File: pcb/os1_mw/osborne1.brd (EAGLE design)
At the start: 147 x 100 mm, 18 parts

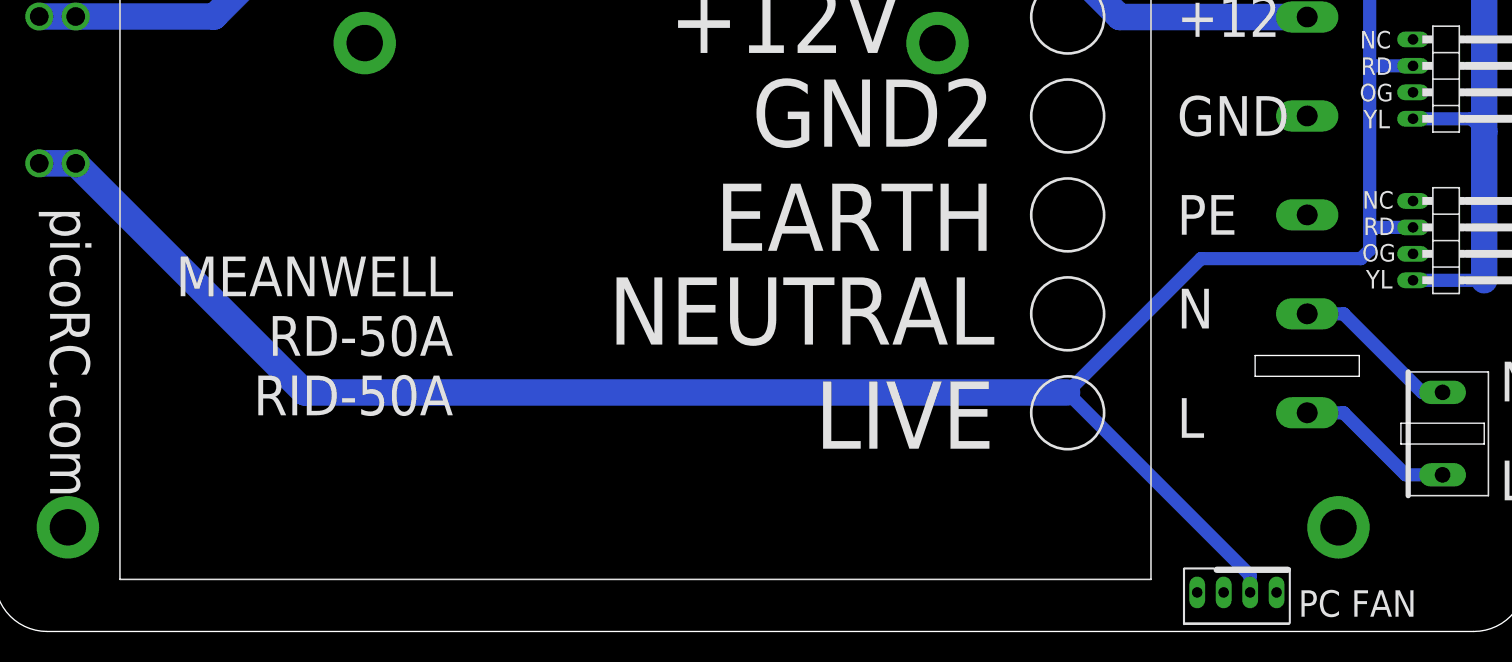
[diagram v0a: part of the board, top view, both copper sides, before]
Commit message: adjust trace spacing
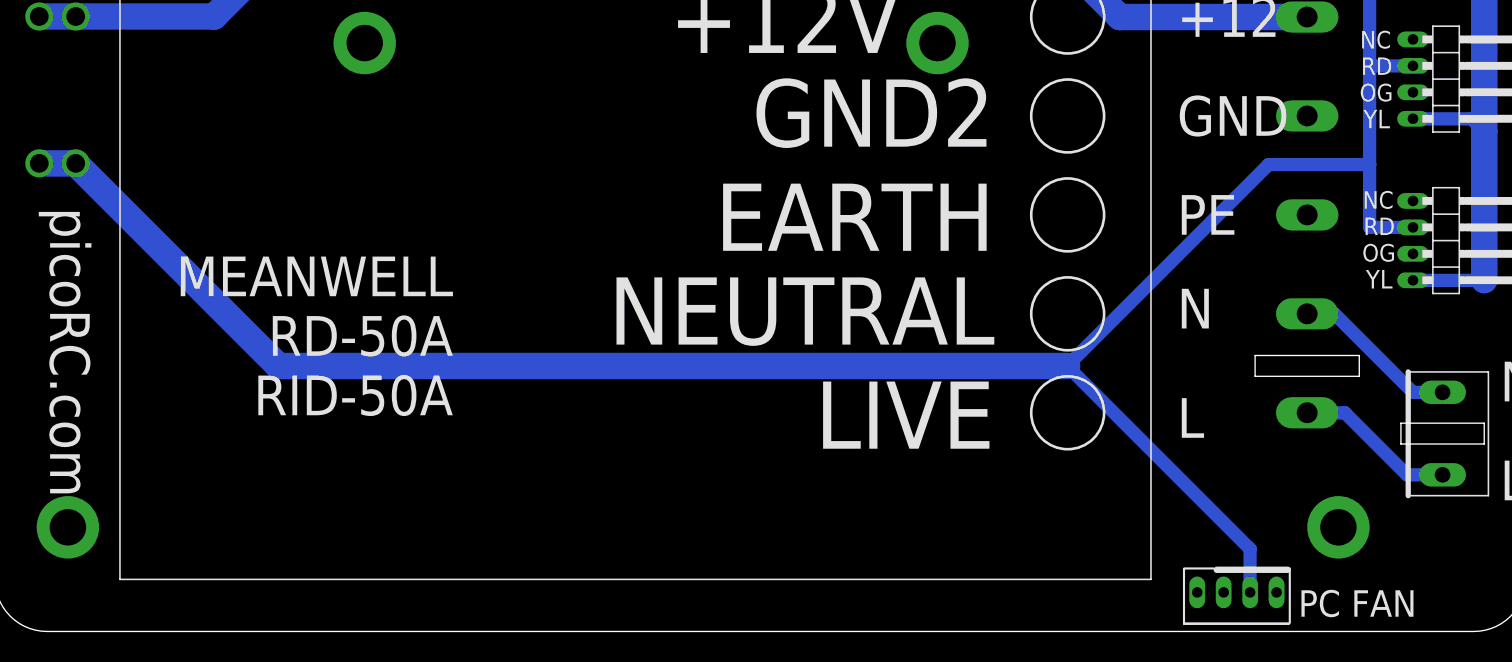
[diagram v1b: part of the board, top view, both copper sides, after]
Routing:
- net +12V: track 213.8 -> 215.4 mm
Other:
- board text added: "YELLOW ORANGE RED NC"
- board text removed: "NC RED ORANGE YELLOW"
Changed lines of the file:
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@@
 <setting verticaltext="up"/>
 </settings>
-<grid distance="5" unitdist="mil" unit="mil" style="lines" multiple="1" display="no" altdistance="1" altunitdist="mil" altunit="mil"/>
+<grid distance="50" unitdist="mil" unit="mil" style="lines" multiple="1" display="no" altdistance="1" altunitdist="mil" altunit="mil"/>
 <layers>
-<layer number="1" name="Top" color="4" fill="1" visible="no" active="yes"/>
+<layer number="1" name="Top" color="4" fill="1" visible="yes" active="yes"/>
 <layer number="2" name="Route2" color="16" fill="1" visible="no" active="no"/>
 <layer number="3" name="Route3" color="17" fill="1" visible="no" active="no"/>
@@
 <text x="132.676" y="54.283" size="1.6764" layer="25" align="center">RD</text>
 <text x="132.565" y="56.823" size="1.6764" layer="25" align="center">NC</text>
-<text x="137.994" y="68.523" size="1.4224" layer="26" distance="80" rot="MR0" align="center-right">NC
+<text x="138.494" y="68.523" size="1.4224" layer="26" distance="80" rot="SMR180" align="center-left">YELLOW
+ORANGE
 RED
-ORANGE
-YELLOW</text>
-<text x="138.121" y="53.013" size="1.4224" layer="26" distance="80" rot="MR0" align="center-right">NC
-RED
-ORANGE
-YELLOW</text>
-<text x="138.248" y="37.503" size="1.4224" layer="26" distance="80" rot="MR0" align="center-right">NC
-RED
-ORANGE
-YELLOW</text>
+NC</text>
 <text x="113.5" y="40" size="3.81" layer="25" align="center-left">PE</text>
 <text x="113.5" y="49.5" size="3.81" layer="25" align="center-left">GND</text>
@@
 <wire x1="123" y1="18" x2="128" y2="18" width="0.508" layer="22"/>
 <wire x1="128" y1="18" x2="135" y2="11" width="0.508" layer="22"/>
-<wire x1="135" y1="11" x2="142" y2="11" width="0.508" layer="22"/>
-<wire x1="142" y1="11" x2="143" y2="12" width="0.508" layer="22"/>
-<wire x1="143" y1="12" x2="143" y2="24" width="0.508" layer="22"/>
-<wire x1="143" y1="24" x2="141" y2="26" width="0.508" layer="22"/>
-<wire x1="141" y1="26" x2="139" y2="26" width="0.508" layer="22"/>
+<wire x1="135" y1="11" x2="142.5" y2="11" width="0.508" layer="22"/>
+<wire x1="142.5" y1="11" x2="143.5" y2="12" width="0.508" layer="22"/>
+<wire x1="143.5" y1="12" x2="143.5" y2="24" width="0.508" layer="22"/>
+<wire x1="143.5" y1="24" x2="141.5" y2="26" width="0.508" layer="22"/>
+<wire x1="141.5" y1="26" x2="139" y2="26" width="0.508" layer="22"/>
 <wire x1="139" y1="26" x2="132" y2="33" width="0.508" layer="22"/>
 <text x="119.5" y="88" size="2.54" layer="25" align="center-left">+</text>
 <text x="134.5" y="85" size="2.54" layer="25" align="center-left">+</text>
 <text x="134.5" y="82" size="2.54" layer="25" align="center-left">+</text>
+<text x="138.494" y="53.023" size="1.4224" layer="26" distance="80" rot="SMR180" align="center-left">YELLOW
+ORANGE
+RED
+NC</text>
+<text x="138.494" y="37.523" size="1.4224" layer="26" distance="80" rot="SMR180" align="center-left">YELLOW
+ORANGE
+RED
+NC</text>
 </plain>
 <attributes>
@@
 <wire x1="136.16" y1="54.31" x2="132.31" y2="54.31" width="1.27" layer="16"/>
 <wire x1="132.31" y1="54.31" x2="132" y2="54" width="1.27" layer="16"/>
-<wire x1="132" y1="36.64" x2="131.16" y2="35.8" width="1.27" layer="16"/>
-<wire x1="132" y1="54" x2="132" y2="38.64" width="1.27" layer="16"/>
-<wire x1="132" y1="38.64" x2="132" y2="36.64" width="1.27" layer="16"/>
-<wire x1="132" y1="38.64" x2="132.16" y2="38.8" width="1.27" layer="16"/>
-<wire x1="132.16" y1="38.8" x2="136.16" y2="38.8" width="1.27" layer="16"/>
 <contactref element="U$7" pad="A1"/>
 <contactref element="U$7" pad="A0"/>
 <wire x1="4.25" y1="44.95" x2="7.75" y2="44.95" width="2.54" layer="16"/>
-<wire x1="102.95" y1="22.95" x2="120.52" y2="5.38" width="1.27" layer="16"/>
-<wire x1="120.52" y1="5.38" x2="120.52" y2="3.75" width="1.27" layer="16"/>
-<wire x1="131.16" y1="35.8" x2="115.8" y2="35.8" width="1.27" layer="16"/>
-<wire x1="115.8" y1="35.8" x2="102.95" y2="22.95" width="1.27" layer="16"/>
-<wire x1="7.75" y1="44.95" x2="29.75" y2="22.95" width="2.54" layer="16"/>
-<wire x1="29.75" y1="22.95" x2="102.95" y2="22.95" width="2.54" layer="16"/>
+<wire x1="120.52" y1="3.75" x2="120.52" y2="7.92" width="1.27" layer="16"/>
+<wire x1="120.52" y1="7.92" x2="102.95" y2="25.49" width="1.27" layer="16"/>
+<wire x1="7.75" y1="44.95" x2="27.21" y2="25.49" width="2.54" layer="16"/>
+<wire x1="27.21" y1="25.49" x2="102.95" y2="25.49" width="2.54" layer="16"/>
+<wire x1="132" y1="54" x2="132" y2="44.831" width="1.27" layer="16"/>
+<wire x1="102.95" y1="25.49" x2="122.291" y2="44.831" width="1.27" layer="16"/>
+<wire x1="122.291" y1="44.831" x2="132" y2="44.831" width="1.27" layer="16"/>
+<wire x1="132" y1="44.831" x2="132" y2="38.8" width="1.27" layer="16"/>
+<wire x1="132" y1="38.8" x2="136.16" y2="38.8" width="1.27" layer="16"/>
 </signal>
 <signal name="N$2">
@@
 <contactref element="U$3" pad="P$6"/>
 <contactref element="U$2" pad="P$2"/>
-<wire x1="139" y1="22.96" x2="137.04" y2="22.96" width="1.27" layer="16"/>
-<wire x1="129.5" y1="30.5" x2="126" y2="30.5" width="1.27" layer="16"/>
-<wire x1="137.04" y1="22.96" x2="129.5" y2="30.5" width="1.27" layer="16"/>
+<wire x1="139" y1="22.96" x2="136.151" y2="22.96" width="1.27" layer="16"/>
+<wire x1="128.611" y1="30.5" x2="126" y2="30.5" width="1.27" layer="16"/>
+<wire x1="136.151" y1="22.96" x2="128.611" y2="30.5" width="1.27" layer="16"/>
 </signal>
 <signal name="N$4">
 <contactref element="U$2" pad="P$1"/>
 <contactref element="U$3" pad="P$7"/>
-<wire x1="139" y1="15.04" x2="135.46" y2="15.04" width="1.27" layer="16"/>
-<wire x1="135.46" y1="15.04" x2="129.5" y2="21" width="1.27" layer="16"/>
-<wire x1="129.5" y1="21" x2="126" y2="21" width="1.27" layer="16"/>
+<wire x1="139" y1="15.04" x2="135.587" y2="15.04" width="1.27" layer="16"/>
+<wire x1="135.587" y1="15.04" x2="129.627" y2="21" width="1.27" layer="16"/>
+<wire x1="129.627" y1="21" x2="126" y2="21" width="1.27" layer="16"/>
 </signal>
 </signals>
